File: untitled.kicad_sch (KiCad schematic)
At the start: 10 parts, among them J1 USB_B, J2 Screw_Terminal_01x08, J4 Conn_02x05_Odd_Even, J5 Conn_01x02_Pin, J6 Conn_01x02_Pin, U2 LM2936-3.3

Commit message: Update
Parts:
- U2: footprint Package_TO_SOT_SMD:TO-252-3_TabPin2 -> Package_TO_SOT_SMD:SOT-223-3_TabPin2
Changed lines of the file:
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@@
 			)
 		)
-		(property "Footprint" "Package_TO_SOT_SMD:TO-252-3_TabPin2"
+		(property "Footprint" "Package_TO_SOT_SMD:SOT-223-3_TabPin2"
 			(at 129.54 92.075 0)
 			(effects

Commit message: Update
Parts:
- C5: value 10uF -> 15uF; Mouser (none) -> 667-10SVP15M
- C7: Mouser (none) -> 603-C0603ZRY5V9BB104
- J1: Mouser (none) -> 523-UE27-BC54-100
- J2: Mouser (none) -> 649-220110-C081A01LF
- J4: footprint Samtect:CON10_2X5_DUK_FTSH_SAI -> Samtect:CON10_2X5_DUK_FTSH_SAI-M; Mouser (none) -> 200-FTSH10501LDVKP
- R5, R6: Mouser (none) -> 603-RC0603FR-13120RL
- U2: Mouser (none) -> 595-LM2936QMP3.3NPB
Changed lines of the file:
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@@
 		)
 	)
-	(label "3.3V"
-		(at 148.59 97.79 0)
+	(global_label "USB_N"
+		(shape bidirectional)
+		(at 82.55 105.41 0)
+		(fields_autoplaced yes)
 		(effects
 			(font
 				(size 1.27 1.27)
 			)
-			(justify left bottom)
-		)
-	)
-	(label "3.3V"
-		(at 209.55 100.33 0)
+			(justify left)
+		)
+		(property "Intersheetrefs" "${INTERSHEET_REFS}"
+			(at 92.7546 105.41 0)
+			(effects
+				(font
+					(size 1.27 1.27)
+				)
+				(justify left)
+				(hide yes)
+			)
+		)
+	)
+	(global_label "5V"
+		(shape output)
+		(at 106.68 88.9 90)
+		(fields_autoplaced yes)
 		(effects
 			(font
 				(size 1.27 1.27)
 			)
-			(justify left bottom)
-		)
-	)
-	(global_label "USB_N"
+			(justify left)
+		)
+		(property "Intersheetrefs" "${INTERSHEET_REFS}"
+			(at 106.68 83.6167 90)
+			(effects
+				(font
+					(size 1.27 1.27)
+				)
+				(justify left)
+				(hide yes)
+			)
+		)
+	)
+	(global_label "CAN1_N"
 		(shape bidirectional)
-		(at 82.55 105.41 0)
+		(at 223.52 39.37 180)
 		(fields_autoplaced yes)
 		(effects
@@
 				(size 1.27 1.27)
 			)
-			(justify left)
+			(justify right)
 		)
 		(property "Intersheetrefs" "${INTERSHEET_REFS}"
-			(at 92.7546 105.41 0)
-			(effects
-				(font
-					(size 1.27 1.27)
-				)
-				(justify left)
-				(hide yes)
-			)
-		)
-	)
-	(global_label "5V"
-		(shape output)
-		(at 106.68 88.9 90)
+			(at 212.2268 39.37 0)
+			(effects
+				(font
+					(size 1.27 1.27)
+				)
+				(justify right)
+				(hide yes)
+			)
+		)
+	)
+	(global_label "CAN2_N"
+		(shape bidirectional)
+		(at 223.52 49.53 180)
 		(fields_autoplaced yes)
 		(effects
@@
 				(size 1.27 1.27)
 			)
-			(justify left)
+			(justify right)
 		)
 		(property "Intersheetrefs" "${INTERSHEET_REFS}"
-			(at 106.68 83.6167 90)
-			(effects
-				(font
-					(size 1.27 1.27)
-				)
-				(justify left)
-				(hide yes)
-			)
-		)
-	)
-	(global_label "CAN1_N"
+			(at 212.2268 49.53 0)
+			(effects
+				(font
+					(size 1.27 1.27)
+				)
+				(justify right)
+				(hide yes)
+			)
+		)
+	)
+	(global_label "CAN2_P"
 		(shape bidirectional)
-		(at 223.52 39.37 180)
+		(at 223.52 46.99 180)
 		(fields_autoplaced yes)
 		(effects
@@
 		)
 		(property "Intersheetrefs" "${INTERSHEET_REFS}"
-			(at 212.2268 39.37 0)
+			(at 212.2873 46.99 0)
 			(effects
 				(font
@@
 		)
 	)
-	(global_label "CAN2_N"
+	(global_label "USB_P"
 		(shape bidirectional)
-		(at 223.52 49.53 180)
+		(at 82.55 102.87 0)
 		(fields_autoplaced yes)
 		(effects
@@
 				(size 1.27 1.27)
 			)
-			(justify right)
+			(justify left)
 		)
 		(property "Intersheetrefs" "${INTERSHEET_REFS}"
-			(at 212.2268 49.53 0)
-			(effects
-				(font
-					(size 1.27 1.27)
-				)
-				(justify right)
-				(hide yes)
-			)
-		)
-	)
-	(global_label "CAN2_P"
-		(shape bidirectional)
-		(at 223.52 46.99 180)
+			(at 92.6941 102.87 0)
+			(effects
+				(font
+					(size 1.27 1.27)
+				)
+				(justify left)
+				(hide yes)
+			)
+		)
+	)
+	(global_label "3.3V"
+		(shape output)
+		(at 156.21 97.79 0)
 		(fields_autoplaced yes)
 		(effects
@@
 				(size 1.27 1.27)
 			)
-			(justify right)
+			(justify left)
 		)
 		(property "Intersheetrefs" "${INTERSHEET_REFS}"
-			(at 212.2873 46.99 0)
-			(effects
-				(font
-					(size 1.27 1.27)
-				)
-				(justify right)
-				(hide yes)
-			)
-		)
-	)
-	(global_label "USB_P"
+			(at 163.3076 97.79 0)
+			(effects
+				(font
+					(size 1.27 1.27)
+				)
+				(justify left)
+				(hide yes)
+			)
+		)
+	)
+	(global_label "CAN1_P"
 		(shape bidirectional)
-		(at 82.55 102.87 0)
+		(at 223.52 36.83 180)
 		(fields_autoplaced yes)
 		(effects
@@
 				(size 1.27 1.27)
 			)
-			(justify left)
+			(justify right)
 		)
 		(property "Intersheetrefs" "${INTERSHEET_REFS}"
-			(at 92.6941 102.87 0)
-			(effects
-				(font
-					(size 1.27 1.27)
-				)
-				(justify left)
-				(hide yes)
-			)
-		)
-	)
-	(global_label "3.3V"
+			(at 212.2873 36.83 0)
+			(effects
+				(font
+					(size 1.27 1.27)
+				)
+				(justify right)
+				(hide yes)
+			)
+		)
+	)
+	(global_label "SWDCLK"
 		(shape output)
-		(at 156.21 97.79 0)
+		(at 229.87 102.87 0)
 		(fields_autoplaced yes)
 		(effects
@@
 		)
 		(property "Intersheetrefs" "${INTERSHEET_REFS}"
-			(at 163.3076 97.79 0)
-			(effects
-				(font
-					(size 1.27 1.27)
-				)
-				(justify left)
-				(hide yes)
-			)
-		)
-	)
-	(global_label "CAN1_P"
-		(shape bidirectional)
-		(at 223.52 36.83 180)
+			(at 240.3542 102.87 0)
+			(effects
+				(font
+					(size 1.27 1.27)
+				)
+				(justify left)
+				(hide yes)
+			)
+		)
+	)
+	(global_label "3.3V"
+		(shape input)
+		(at 207.01 100.33 180)
 		(fields_autoplaced yes)
 		(effects
@@
 		)
 		(property "Intersheetrefs" "${INTERSHEET_REFS}"
-			(at 212.2873 36.83 0)
+			(at 199.9124 100.33 0)
 			(effects
 				(font
@@
 				)
 				(justify right)
-				(hide yes)
-			)
-		)
-	)
-	(global_label "SWDCLK"
-		(shape output)
-		(at 229.87 102.87 0)
-		(fields_autoplaced yes)
-		(effects
-			(font
-				(size 1.27 1.27)
-			)
-			(justify left)
-		)
-		(property "Intersheetrefs" "${INTERSHEET_REFS}"
-			(at 240.3542 102.87 0)
-			(effects
-				(font
-					(size 1.27 1.27)
-				)
-				(justify left)
 				(hide yes)
 			)
@@
 			)
 		)
+		(property "Mouser" "603-RC0603FR-13120RL"
+			(at 191.77 52.07 0)
+			(effects
+				(font
+					(size 1.27 1.27)
+				)
+				(hide yes)
+			)
+		)
 		(pin "2"
 		)
@@
 			)
 		)
+		(property "Mouser" "649-220110-C081A01LF"
+			(at 236.22 44.45 0)
+			(effects
+				(font
+					(size 1.27 1.27)
+				)
+				(hide yes)
+			)
+		)
 		(pin "1"
 		)
@@
 			)
 		)
+		(property "Mouser" "595-LM2936QMP3.3NPB"
+			(at 129.54 97.79 0)
+			(effects
+				(font
+					(size 1.27 1.27)
+				)
+				(hide yes)
+			)
+		)
 		(pin "3"
 		)
@@
 			)
 		)
+		(property "Mouser" "603-RC0603FR-13120RL"
+			(at 191.77 35.56 0)
+			(effects
+				(font
+					(size 1.27 1.27)
+				)
+				(hide yes)
+			)
+		)
 		(pin "2"
 		)
@@
 			)
 		)
+		(property "Mouser" "603-C0603ZRY5V9BB104"
+			(at 144.78 101.6 0)
+			(effects
+				(font
+					(size 1.27 1.27)
+				)
+				(hide yes)
+			)
+		)
 		(pin "2"
 		)
@@
 			)
 		)
+		(property "Mouser" "523-UE27-BC54-100"
+			(at 68.58 102.87 0)
+			(effects
+				(font
+					(size 1.27 1.27)
+				)
+				(hide yes)
+			)
+		)
 		(pin "3"
 		)
@@
 			)
 		)
-		(property "Footprint" "Samtect:CON10_2X5_DUK_FTSH_SAI"
+		(property "Footprint" "Samtect:CON10_2X5_DUK_FTSH_SAI-M"
 			(at 222.25 105.41 0)
 			(effects
@@
 		)
 		(property "Description" "Generic connector, double row, 02x05, odd/even pin numbering scheme (row 1 odd numbers, row 2 even numbers), script generated (kicad-library-utils/schlib/autogen/connector/)"
+			(at 222.25 105.41 0)
+			(effects
+				(font
+					(size 1.27 1.27)
+				)
+				(hide yes)
+			)
+		)
+		(property "Mouser" "200-FTSH10501LDVKP"
 			(at 222.25 105.41 0)
 			(effects
@@
 			)
 		)
-		(property "Value" "10uF"
+		(property "Value" "15uF"
 			(at 110.49 106.0449 0)
 			(effects
@@
 			(at 106.68 105.41 0)
 			(effects
+				(font
+					(size 1.27 1.27)
+				)
+				(hide yes)
+			)
+		)
+		(property "Mouser" "667-10SVP15M"
+			(at 106.68 105.41 0)
+			(effects

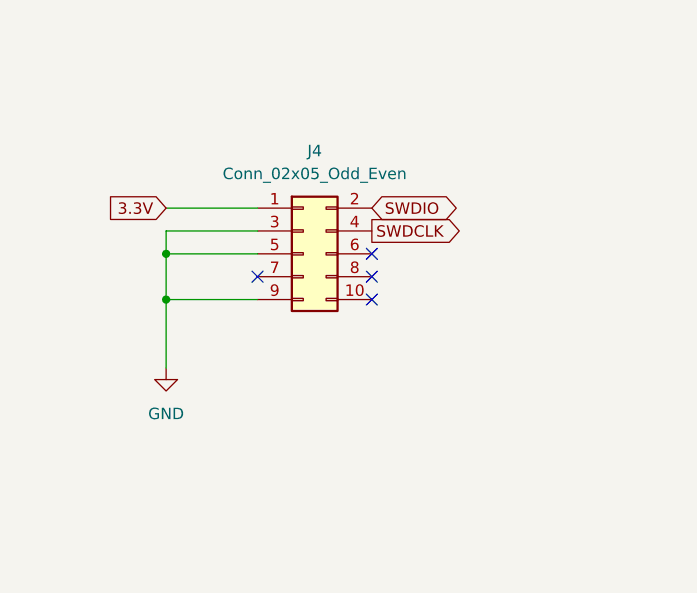
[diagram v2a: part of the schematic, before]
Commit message: Added an alternative 4-pin debug header
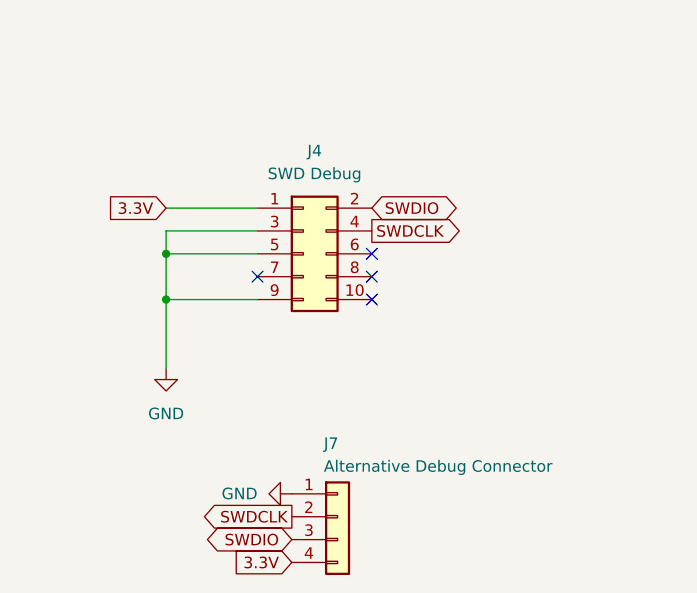
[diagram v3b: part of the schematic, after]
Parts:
- added J7: Alternative Debug Connector, Connector_PinHeader_2.54mm:PinHeader_1x04_P2.54mm_Vertical, symbol Connector_Generic:Conn_01x04
- J4: value Conn_02x05_Odd_Even -> SWD Debug
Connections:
- net 3.3V: now also J7.4 (Pin_4)
- net GND: now also J7.1 (Pin_1)
- net SWDCLK: now also J7.2 (Pin_2)
- net SWDIO: now also J7.3 (Pin_3)
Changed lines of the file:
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@@
+	)
+	(global_label "3.3V"
+		(shape input)
+		(at 220.98 139.7 180)
+		(fields_autoplaced yes)
+		(effects
+			(font
+				(size 1.27 1.27)
+			)
+			(justify right)
+		)
+		(property "Intersheetrefs" "${INTERSHEET_REFS}"
+			(at 213.8824 139.7 0)
+			(effects
+				(font
+					(size 1.27 1.27)
+				)
+				(justify right)
+				(hide yes)
+			)
+		)
 	)
 	(global_label "3.3V"
@@
 	(global_label "SWDIO"
 		(shape bidirectional)
-		(at 229.87 100.33 0)
+		(at 220.98 137.16 180)
 		(fields_autoplaced yes)
 		(effects
@@
 				(size 1.27 1.27)
 			)
+			(justify right)
+		)
+		(property "Intersheetrefs" "${INTERSHEET_REFS}"
+			(at 211.0173 137.16 0)
+			(effects
+				(font
+					(size 1.27 1.27)
+				)
+				(justify right)
+				(hide yes)
+			)
+		)
+	)
+	(global_label "SWDCLK"
+		(shape output)
+		(at 220.98 134.62 180)
+		(fields_autoplaced yes)
+		(effects
+			(font
+				(size 1.27 1.27)
+			)
+			(justify right)
+		)
+		(property "Intersheetrefs" "${INTERSHEET_REFS}"
+			(at 210.4958 134.62 0)
+			(effects
+				(font
+					(size 1.27 1.27)
+				)
+				(justify right)
+				(hide yes)
+			)
+		)
+	)
+	(global_label "SWDIO"
+		(shape bidirectional)
+		(at 229.87 100.33 0)
+		(fields_autoplaced yes)
+		(effects
+			(font
+				(size 1.27 1.27)
+			)
 			(justify left)
 		)
@@
 	)
 	(symbol
+		(lib_id "power:GND")
+		(at 220.98 132.08 270)
+		(unit 1)
+		(exclude_from_sim no)
+		(in_bom yes)
+		(on_board yes)
+		(dnp no)
+		(fields_autoplaced yes)
+		(property "Reference" "#PWR014"
+			(at 214.63 132.08 0)
+			(effects
+				(font
+					(size 1.27 1.27)
+				)
+				(hide yes)
+			)
+		)
+		(property "Value" "GND"
+			(at 217.17 132.0799 90)
+			(effects
+				(font
+					(size 1.27 1.27)
+				)
+				(justify right)
+			)
+		)
+		(property "Footprint" ""
+			(at 220.98 132.08 0)
+			(effects
+				(font
+					(size 1.27 1.27)
+				)
+				(hide yes)
+			)
+		)
+		(property "Datasheet" ""
+			(at 220.98 132.08 0)
+			(effects
+				(font
+					(size 1.27 1.27)
+				)
+				(hide yes)
+			)
+		)
+		(property "Description" "Power symbol creates a global label with name \"GND\" , ground"
+			(at 220.98 132.08 0)
+			(effects
+				(font
+					(size 1.27 1.27)
+				)
+				(hide yes)
+			)
+		)
+		(pin "1"
+		)
+		(instances
+			(project "USBCAN-X2"
+				(path "/545a5907-9f92-4fcd-ad93-c3335194e6e8/febb179f-73ed-41de-a11e-91fdb2e67b79"
+					(reference "#PWR014")
+					(unit 1)
+				)
+			)
+		)
+	)
+	(symbol
 		(lib_id "Device:C")
 		(at 144.78 101.6 0)
@@
 			)
 		)
-		(property "Value" "Conn_02x05_Odd_Even"
+		(property "Value" "SWD  Debug"
 			(at 223.52 96.52 0)
 			(effects
@@
 					(unit 1)
 				)
+			)
+		)
+	)
+	(symbol
+		(lib_id "Connector_Generic:Conn_01x04")
+		(at 226.06 134.62 0)
+		(unit 1)
+		(exclude_from_sim no)
+		(in_bom yes)
+		(on_board yes)
+		(dnp no)
+		(property "Reference" "J7"
+			(at 224.536 126.492 0)
+			(effects
+				(font
+					(size 1.27 1.27)
+				)
+				(justify left)
+			)
+		)
+		(property "Value" "Alternative Debug Connector"
+			(at 224.536 129.032 0)
+			(effects
+				(font
+					(size 1.27 1.27)
+				)
+				(justify left)
+			)
+		)
+		(property "Footprint" "Connector_PinHeader_2.54mm:PinHeader_1x04_P2.54mm_Vertical"
+			(at 226.06 134.62 0)
+			(effects
+				(font
+					(size 1.27 1.27)
+				)
+				(hide yes)
+			)
+		)
+		(property "Datasheet" "~"
+			(at 226.06 134.62 0)
+			(effects
+				(font
+					(size 1.27 1.27)
+				)
+				(hide yes)
+			)
+		)
+		(property "Description" "Generic connector, single row, 01x04, script generated (kicad-library-utils/schlib/autogen/connector/)"
+			(at 226.06 134.62 0)
+			(effects
+				(font
+					(size 1.27 1.27)
+				)
+				(hide yes)
+			)
+		)
+		(pin "1"
+		)
+		(pin "2"
+		)
+		(pin "3"
+		)
+		(pin "4"
+		)
+		(instances
+			(project ""
+				(path "/545a5907-9f92-4fcd-ad93-c3335194e6e8/febb179f-73ed-41de-a11e-91fdb2e67b79"
+					(reference "J7")
+					(unit 1)
+				)

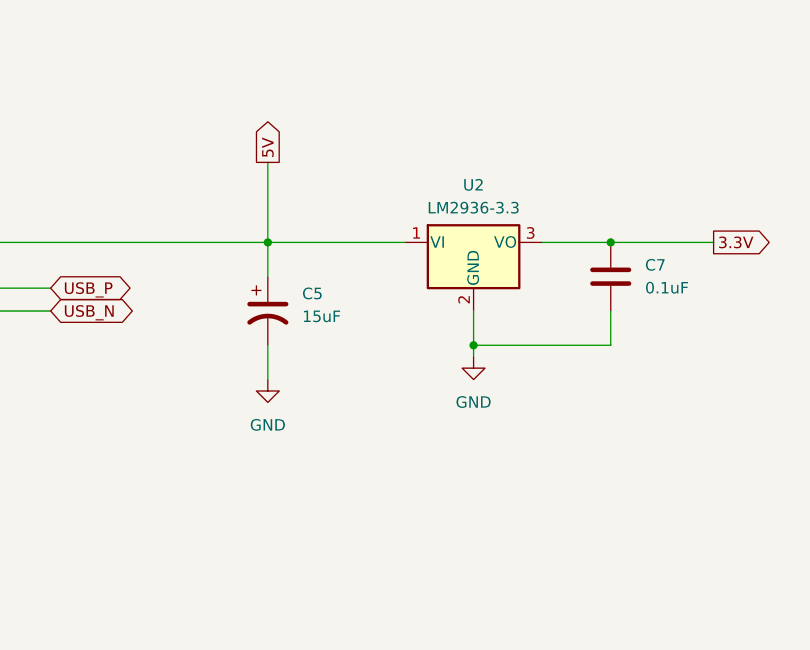
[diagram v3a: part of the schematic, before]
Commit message: Add pull-up to NRST
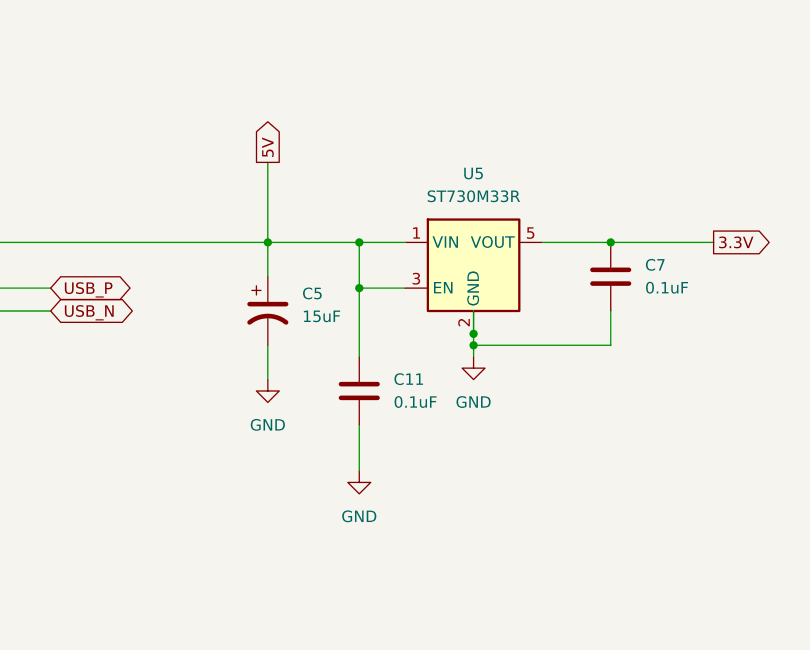
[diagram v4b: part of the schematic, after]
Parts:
- removed U2: LM2936-3.3, Package_TO_SOT_SMD:SOT-223-3_TabPin2, symbol Regulator_Linear:LM2936-3.3
- added C11: 0.1uF, Capacitor_SMD:C_0603_1608Metric, symbol Device:C
- added U5: ST730M33R, Package_TO_SOT_SMD:SOT-23-5, symbol Regulator_Linear:NCP163ASN330T1G
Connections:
- net 3.3V: now also U5.5 (VOUT)
- net 5V: now also C11.1, U5.1 (VIN), U5.3 (EN)
- net GND: now also C11.2, U5.2 (GND)

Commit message: Clean some tracks up.
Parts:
- J5, J6: value Conn_01x02_Pin -> 2-pin header
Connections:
- net CAN1_N: no longer J2.3 (Pin_3)
- net CAN2_N: no longer J2.7 (Pin_7)
- net GND: now also J2.4 (Pin_4), J2.8 (Pin_8)
- net at J5.2 (Pin_2), R6.2: no longer J2.8 (Pin_8)
- net at J6.2 (Pin_2), R5.2: no longer J2.4 (Pin_4)
- no-connect marks 4 -> 6
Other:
- moved on the sheet: J5, J6, R5, R6
